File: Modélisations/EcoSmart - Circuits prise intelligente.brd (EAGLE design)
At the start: 291.7 x 131.6 mm, 8 parts, among them U1 ARDUINO-UNO-R3-SHIELD

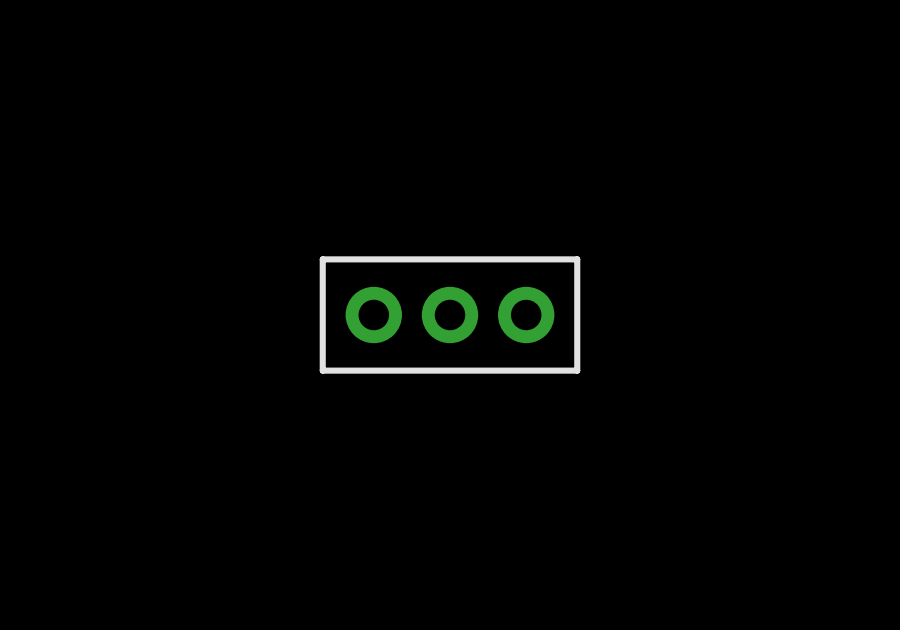
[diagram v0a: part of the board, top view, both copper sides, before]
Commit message: remove slide switch
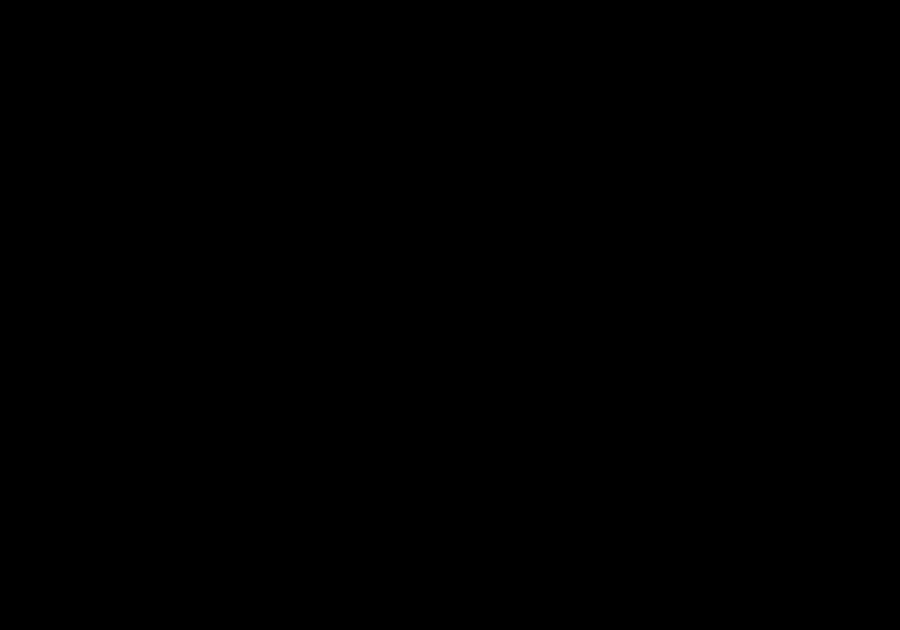
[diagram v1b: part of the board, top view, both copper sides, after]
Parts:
- removed S2: TOGGLE, Tinkercad:SWITCH-SPDT-PTH-8.5X3.7MM
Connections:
- removed net U1_D4: S2.3, U1.D4
- net BAT3-: no longer S2.1
